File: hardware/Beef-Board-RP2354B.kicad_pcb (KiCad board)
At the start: 2 copper layers, 84 x 59.2 mm, 81 parts, among them J1 USB-C DEVICE, J10 VAUX OUT, J11 B1 LEGACY, J12 B2 LEGACY, J13 B3 LEGACY, J14 B4 LEGACY, J15 B5 LEGACY, J16 B6 LEGACY, J17 B7 LEGACY, J18 B8 LEGACY, J19 B9 LEGACY, J2 POWER SELECT, J20 B10 LEGACY, J21 B11 LEGACY, J22 USB COMMON, J3 VAUX 5V INPUT, J31 ENCODER 1, J32 ENCODER 2, J33 AE1 0-5V, J34 AE2 0-5V, J4 USB-C AUX POWER, J40 TT RGB, J41 CENTER BAR RGB, J42 UART A 3V3, J43 UART B 3V3, J5 ENC1 A, J6 ENC1 B, J60 BOOTSEL HEADER, J61 RESET HEADER, J7 ENC2 A, J8 ENC2 B, J9 VAUX OUT, Q1 2N7002, Q10 2N7002, Q11 2N7002, Q2 2N7002, Q3 2N7002, Q4 2N7002, Q5 2N7002, Q6 2N7002, Q7 2N7002, Q8 2N7002, Q9 2N7002, U1 RP2354B, U2 USBLC6-2SC6, U3 AP2112K-3.3, Y1 12MHz CL=10pF

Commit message: Revert "Replace power switch with selectable header"
This reverts commit b092bcadf7da63c17735a3d5c7bcba7038b5f74d.
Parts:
- removed J2: POWER SELECT, PinHeader_1x03_P2.54mm_Vertical
- added SW1: POWER SELECT, Button_Switch_THT:SW_DIP_SPSTx01_Slide_9.78x4.72mm_W7.62mm_P2.54mm, F.Cu at (155.8, 105.9)
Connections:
- D1 pad 1: J4_SEL_5V -> /VAUX_5V
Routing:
- net J4_SEL_5V: track 49.9 -> 0.00 mm, vias 1 -> 0
- net /VAUX_5V: track 137.7 -> 142.2 mm
- net /VBUS_5V: track 153.9 -> 149.7 mm

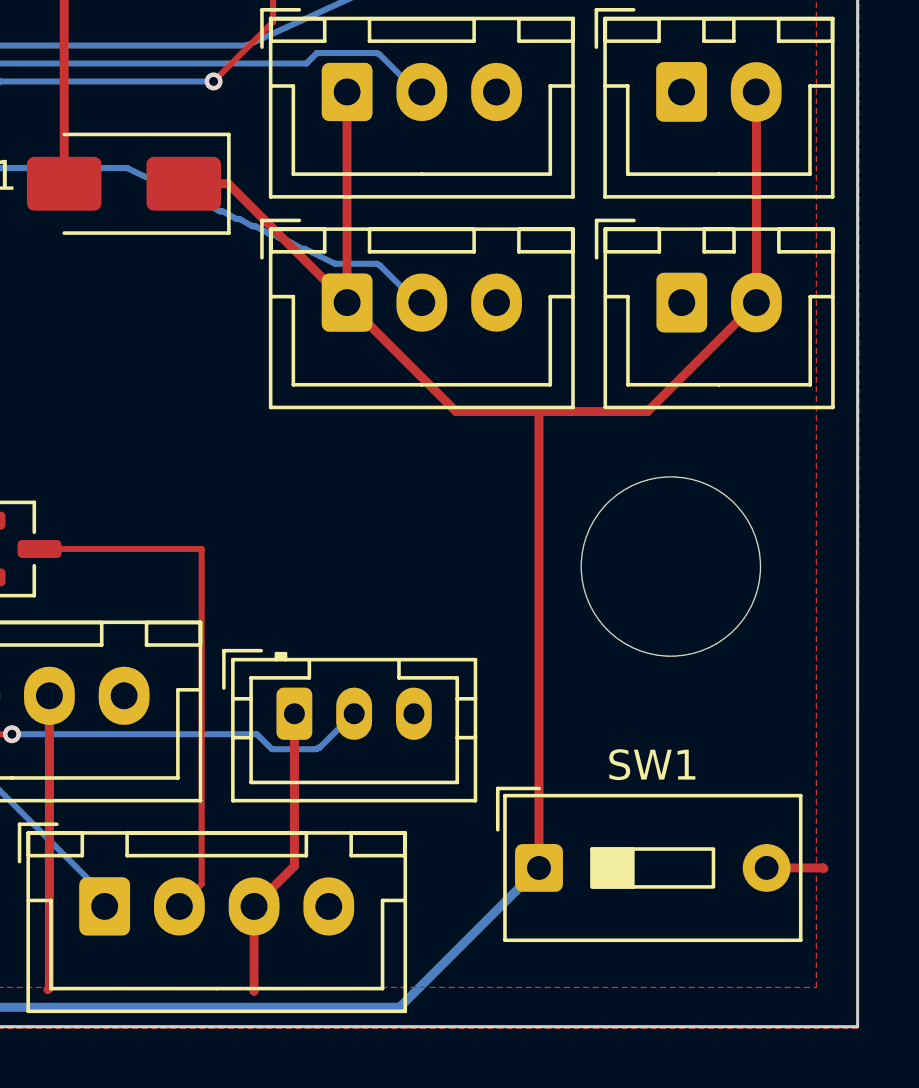
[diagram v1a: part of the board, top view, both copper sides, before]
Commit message: Replace power switch with selectable header
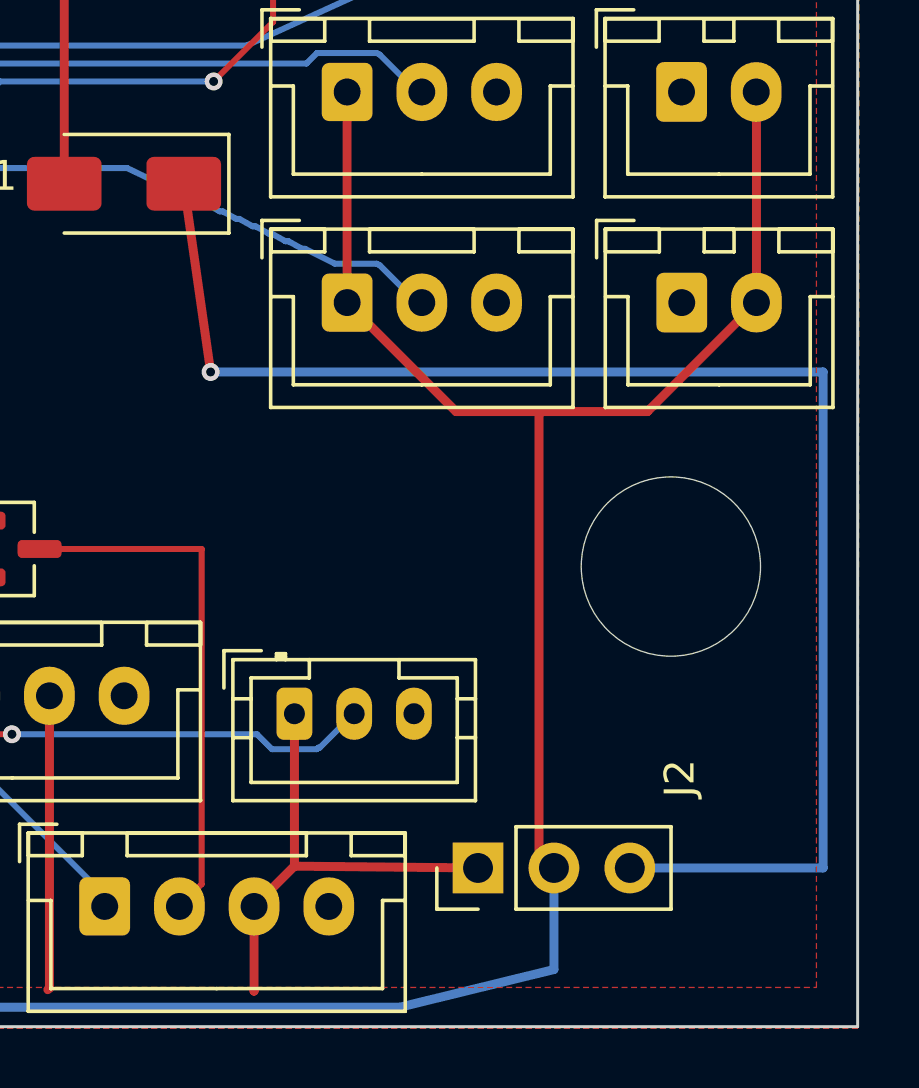
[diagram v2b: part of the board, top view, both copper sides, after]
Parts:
- removed SW1: POWER SELECT, Button_Switch_THT:SW_DIP_SPSTx01_Slide_9.78x4.72mm_W7.62mm_P2.54mm
- added J2: POWER SELECT, PinHeader_1x03_P2.54mm_Vertical, F.Cu at (153.8, 105.9)
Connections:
- D1 pad 1: /VAUX_5V -> J4_SEL_5V
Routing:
- net J4_SEL_5V: track 0.00 -> 49.9 mm, vias 0 -> 1
- net /VAUX_5V: track 142.2 -> 137.7 mm
- net /VBUS_5V: track 149.7 -> 153.9 mm
